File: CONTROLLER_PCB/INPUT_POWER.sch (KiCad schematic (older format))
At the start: 14 parts

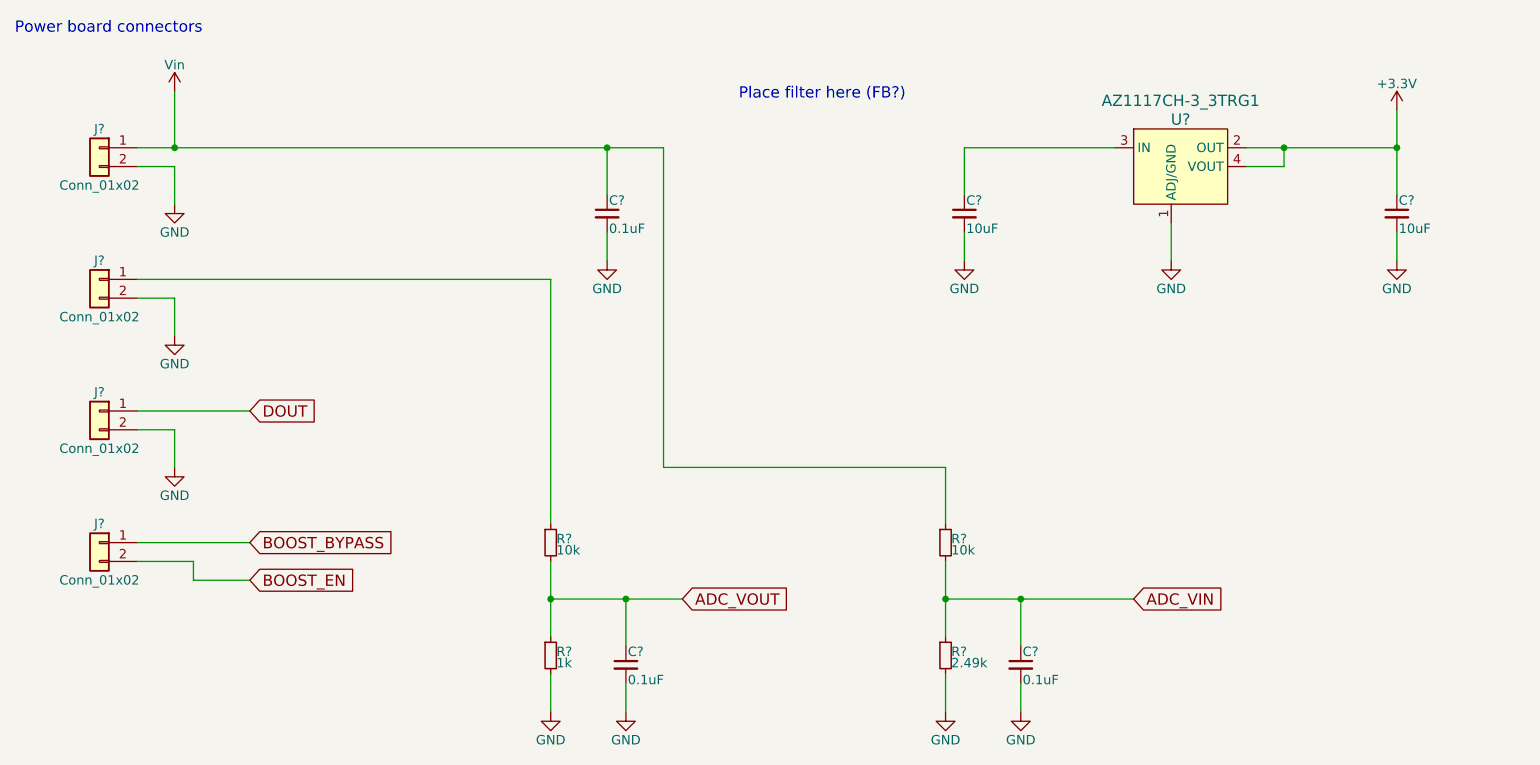
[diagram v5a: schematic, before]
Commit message: Updated POWER_PCB & CONTROLLER_PCB sch's and layouts
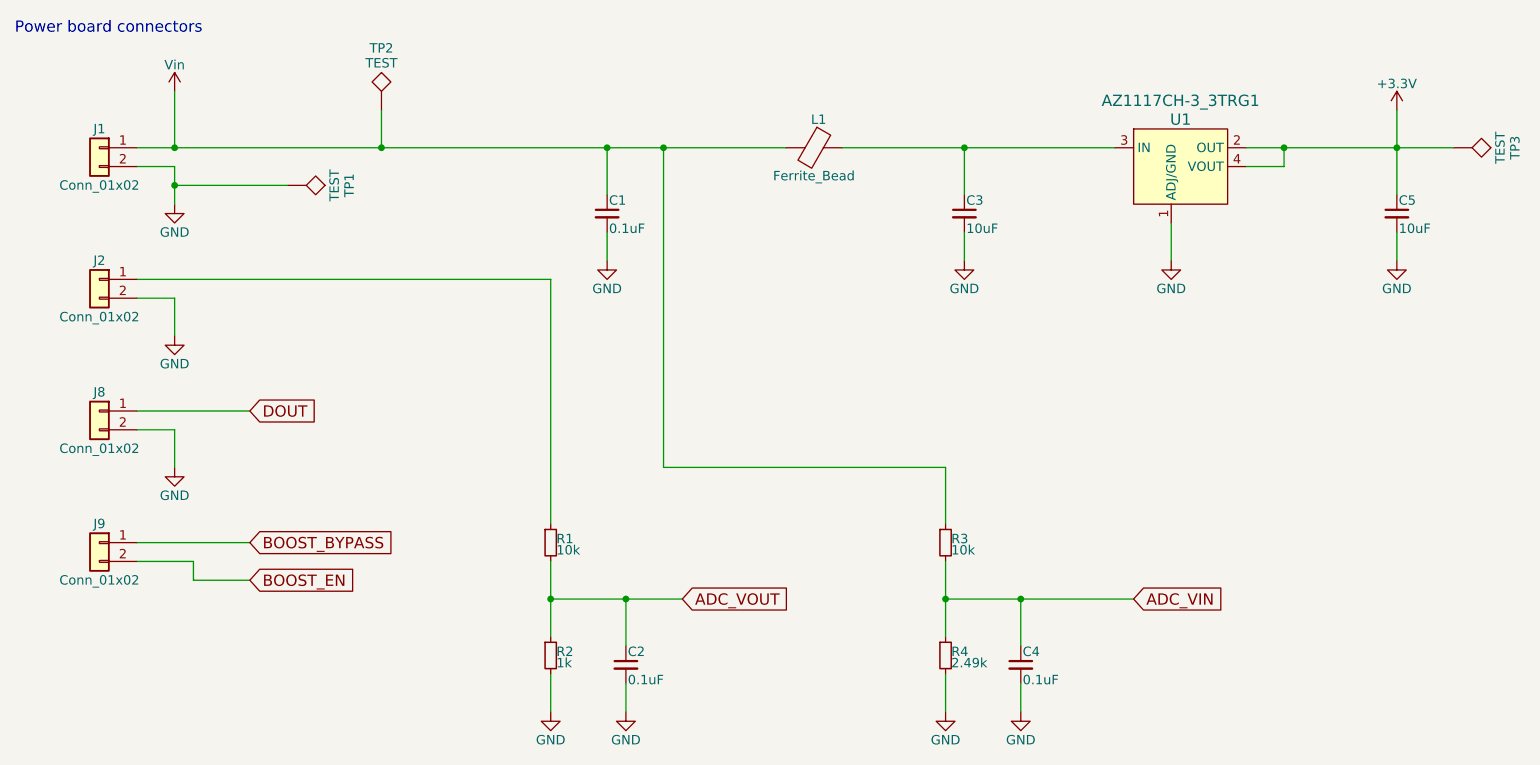
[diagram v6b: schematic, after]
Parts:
- added L1: Ferrite_Bead, Capacitors_SMD:C_0805_HandSoldering, symbol Ferrite_Bead
- added TP1, TP2, TP3: TEST, Measurement_Points:Measurement_Point_Round-SMD-Pad_Small, symbol TEST
- J1, J2, J8, J9: renamed from J?; footprint (none) -> Pin_Headers:Pin_Header_Straight_1x02_Pitch2.54mm
- gave numbers to parts that had none: 10
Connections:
- net +3V3: now also TP3.1
- net GND: now also TP1.1
- net Vin: now also L1.2, TP2.1
- net at C3.1, U1.3 (IN): now also L1.1
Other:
- note removed: "Place filter here (FB?)"
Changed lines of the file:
@@
 $EndDescr
 $Comp
-L Conn_01x02 J?
+L Conn_01x02 J1
 U 1 1 5C71F1FE
 P 2300 1600
-F 0 "J?" H 2300 1700 50  0000 C CNN
+F 0 "J1" H 2300 1700 50  0000 C CNN
 F 1 "Conn_01x02" H 2300 1400 50  0000 C CNN
-F 2 "" H 2300 1600 50  0001 C CNN
+F 2 "Pin_Headers:Pin_Header_Straight_1x02_Pitch2.54mm" H 2300 1600 50  0001 C CNN
 F 3 "" H 2300 1600 50  0001 C CNN
 	1    2300 1600
@@
 $EndComp
 $Comp
-L Conn_01x02 J?
+L Conn_01x02 J2
 U 1 1 5C71F1FF
 P 2300 2300
-F 0 "J?" H 2300 2400 50  0000 C CNN
+F 0 "J2" H 2300 2400 50  0000 C CNN
 F 1 "Conn_01x02" H 2300 2100 50  0000 C CNN
-F 2 "" H 2300 2300 50  0001 C CNN
+F 2 "Pin_Headers:Pin_Header_Straight_1x02_Pitch2.54mm" H 2300 2300 50  0001 C CNN
 F 3 "" H 2300 2300 50  0001 C CNN
 	1    2300 2300
@@
 $EndComp
 $Comp
-L Conn_01x02 J?
+L Conn_01x02 J8
 U 1 1 5C71F200
 P 2300 3000
-F 0 "J?" H 2300 3100 50  0000 C CNN
+F 0 "J8" H 2300 3100 50  0000 C CNN
 F 1 "Conn_01x02" H 2300 2800 50  0000 C CNN
-F 2 "" H 2300 3000 50  0001 C CNN
+F 2 "Pin_Headers:Pin_Header_Straight_1x02_Pitch2.54mm" H 2300 3000 50  0001 C CNN
 F 3 "" H 2300 3000 50  0001 C CNN
 	1    2300 3000
@@
 $EndComp
 $Comp
-L GND #PWR?
+L GND #PWR01
 U 1 1 5C71F201
 P 2700 1900
-F 0 "#PWR?" H 2700 1650 50  0001 C CNN
+F 0 "#PWR01" H 2700 1650 50  0001 C CNN
 F 1 "GND" H 2700 1750 50  0000 C CNN
 F 2 "" H 2700 1900 50  0001 C CNN
@@
 	2700 1700 2700 1900
 $Comp
-L Vin #PWR?
+L Vin #PWR02
 U 1 1 5C71F202
 P 2700 1300
-F 0 "#PWR?" H 2700 1150 50  0001 C CNN
+F 0 "#PWR02" H 2700 1150 50  0001 C CNN
 F 1 "Vin" H 2700 1440 50  0000 C CNN
 F 2 "" H 2700 1300 50  0001 C CNN
@@
 	2700 1300 2700 1600
 $Comp
-L Conn_01x02 J?
+L Conn_01x02 J9
 U 1 1 5C71F203
 P 2300 3700
-F 0 "J?" H 2300 3800 50  0000 C CNN
+F 0 "J9" H 2300 3800 50  0000 C CNN
 F 1 "Conn_01x02" H 2300 3500 50  0000 C CNN
-F 2 "" H 2300 3700 50  0001 C CNN
+F 2 "Pin_Headers:Pin_Header_Straight_1x02_Pitch2.54mm" H 2300 3700 50  0001 C CNN
 F 3 "" H 2300 3700 50  0001 C CNN
 	1    2300 3700
@@
 $EndComp
 $Comp
-L GND #PWR?
+L GND #PWR03
 U 1 1 5C71F204
 P 2700 2600
-F 0 "#PWR?" H 2700 2350 50  0001 C CNN
+F 0 "#PWR03" H 2700 2350 50  0001 C CNN
 F 1 "GND" H 2700 2450 50  0000 C CNN
 F 2 "" H 2700 2600 50  0001 C CNN
@@
 	2700 1700 2500 1700
 Wire Wire Line
-	2500 1600 5300 1600
-$Comp
-L GND #PWR?
+	2500 1600 5950 1600
+$Comp
+L GND #PWR04
 U 1 1 5C71F205
 P 2700 3300
-F 0 "#PWR?" H 2700 3050 50  0001 C CNN
+F 0 "#PWR04" H 2700 3050 50  0001 C CNN
 F 1 "GND" H 2700 3150 50  0000 C CNN
 F 2 "" H 2700 3300 50  0001 C CNN
@@
 Power board connectors
 $Comp
-L AZ1117CH-3_3TRG1 U?
+L AZ1117CH-3_3TRG1 U1
 U 1 1 5C71F57F
 P 8000 1600
-F 0 "U?" H 8050 1750 60  0000 C CNN
+F 0 "U1" H 8050 1750 60  0000 C CNN
 F 1 "AZ1117CH-3_3TRG1" H 8050 1850 60  0000 C CNN
 F 2 "digikey-footprints:SOT-223" H 8200 1800 60  0001 L CNN
@@
 $EndComp
 $Comp
-L C_Small C?
+L C_Small C3
 U 1 1 5C71F6FE
 P 6900 1950
-F 0 "C?" H 6910 2020 50  0000 L CNN
+F 0 "C3" H 6910 2020 50  0000 L CNN
 F 1 "10uF" H 6910 1870 50  0000 L CNN
 F 2 "Capacitors_SMD:C_0805_HandSoldering" H 6900 1950 50  0001 C CNN
@@
 $EndComp
 $Comp
-L GND #PWR?
+L GND #PWR05
 U 1 1 5C71F705
 P 6900 2200
-F 0 "#PWR?" H 6900 1950 50  0001 C CNN
+F 0 "#PWR05" H 6900 1950 50  0001 C CNN
 F 1 "GND" H 6900 2050 50  0000 C CNN
 F 2 "" H 6900 2200 50  0001 C CNN
@@
 $EndComp
 $Comp
-L +3.3V #PWR?
+L +3.3V #PWR06
 U 1 1 5C71F70B
 P 9200 1400
-F 0 "#PWR?" H 9200 1250 50  0001 C CNN
+F 0 "#PWR06" H 9200 1250 50  0001 C CNN
 F 1 "+3.3V" H 9200 1540 50  0000 C CNN
 F 2 "" H 9200 1400 50  0001 C CNN
@@
 	6900 2050 6900 2200
 $Comp
-L C_Small C?
+L C_Small C5
 U 1 1 5C71F7B4
 P 9200 1950
-F 0 "C?" H 9210 2020 50  0000 L CNN
+F 0 "C5" H 9210 2020 50  0000 L CNN
 F 1 "10uF" H 9210 1870 50  0000 L CNN
 F 2 "Capacitors_SMD:C_0805_HandSoldering" H 9200 1950 50  0001 C CNN
@@
 $EndComp
 $Comp
-L GND #PWR?
+L GND #PWR07
 U 1 1 5C71F7BA
 P 9200 2200
-F 0 "#PWR?" H 9200 1950 50  0001 C CNN
+F 0 "#PWR07" H 9200 1950 50  0001 C CNN
 F 1 "GND" H 9200 2050 50  0000 C CNN
 F 2 "" H 9200 2200 50  0001 C CNN
@@
 	9200 2050 9200 2200
 $Comp
-L GND #PWR?
+L GND #PWR08
 U 1 1 5C71F7DD
 P 8000 2200
-F 0 "#PWR?" H 8000 1950 50  0001 C CNN
+F 0 "#PWR08" H 8000 1950 50  0001 C CNN
 F 1 "GND" H 8000 2050 50  0000 C CNN
 F 2 "" H 8000 2200 50  0001 C CNN
@@
 	8000 2000 8000 2200
 Wire Wire Line
-	8400 1600 9200 1600
+	8400 1600 9500 1600
 Connection ~ 9200 1600
 Wire Wire Line
@@
 Connection ~ 8600 1600
 Wire Wire Line
-	7700 1600 6900 1600
-$Comp
-L R_Small R?
+	6250 1600 7700 1600
+$Comp
+L R_Small R1
 U 1 1 5C71FC58
 P 4700 3700
-F 0 "R?" H 4730 3720 50  0000 L CNN
+F 0 "R1" H 4730 3720 50  0000 L CNN
 F 1 "10k" H 4730 3660 50  0000 L CNN
 F 2 "Resistors_SMD:R_0603_HandSoldering" H 4700 3700 50  0001 C CNN
@@
 $EndComp
 $Comp
-L R_Small R?
+L R_Small R2
 U 1 1 5C71FC9D
 P 4700 4300
-F 0 "R?" H 4730 4320 50  0000 L CNN
+F 0 "R2" H 4730 4320 50  0000 L CNN
 F 1 "1k" H 4730 4260 50  0000 L CNN
 F 2 "Resistors_SMD:R_0603_HandSoldering" H 4700 4300 50  0001 C CNN
@@
 $EndComp
 $Comp
-L C_Small C?
+L C_Small C2
 U 1 1 5C71FF06
 P 5100 4350
-F 0 "C?" H 5110 4420 50  0000 L CNN
+F 0 "C2" H 5110 4420 50  0000 L CNN
 F 1 "0.1uF" H 5110 4270 50  0000 L CNN
 F 2 "Capacitors_SMD:C_0603_HandSoldering" H 5100 4350 50  0001 C CNN
@@
 $EndComp
 $Comp
-L GND #PWR?
+L GND #PWR09
 U 1 1 5C71FF0D
 P 5100 4600
-F 0 "#PWR?" H 5100 4350 50  0001 C CNN
+F 0 "#PWR09" H 5100 4350 50  0001 C CNN
 F 1 "GND" H 5100 4450 50  0000 C CNN
 F 2 "" H 5100 4600 50  0001 C CNN
@@
 	5100 4450 5100 4600
 $Comp
-L R_Small R?
+L R_Small R3
 U 1 1 5C72000B
 P 6800 3700
-F 0 "R?" H 6830 3720 50  0000 L CNN
+F 0 "R3" H 6830 3720 50  0000 L CNN
 F 1 "10k" H 6830 3660 50  0000 L CNN
 F 2 "Resistors_SMD:R_0603_HandSoldering" H 6800 3700 50  0001 C CNN
@@
 $EndComp
 $Comp
-L R_Small R?
+L R_Small R4
 U 1 1 5C720011
 P 6800 4300
-F 0 "R?" H 6830 4320 50  0000 L CNN
+F 0 "R4" H 6830 4320 50  0000 L CNN
 F 1 "2.49k" H 6830 4260 50  0000 L CNN
 F 2 "Resistors_SMD:R_0603_HandSoldering" H 6800 4300 50  0001 C CNN
@@
 $EndComp
 $Comp
-L C_Small C?
+L C_Small C4
 U 1 1 5C720017
 P 7200 4350
-F 0 "C?" H 7210 4420 50  0000 L CNN
+F 0 "C4" H 7210 4420 50  0000 L CNN
 F 1 "0.1uF" H 7210 4270 50  0000 L CNN
 F 2 "Capacitors_SMD:C_0603_HandSoldering" H 7200 4350 50  0001 C CNN
@@
 $EndComp
 $Comp
-L GND #PWR?
+L GND #PWR010
 U 1 1 5C72001D
 P 7200 4600
-F 0 "#PWR?" H 7200 4350 50  0001 C CNN
+F 0 "#PWR010" H 7200 4350 50  0001 C CNN
 F 1 "GND" H 7200 4450 50  0000 C CNN
 F 2 "" H 7200 4600 50  0001 C CNN
@@
 	4700 2300 4700 3600
 $Comp
-L GND #PWR?
+L GND #PWR011
 U 1 1 5C720067
 P 4700 4600
-F 0 "#PWR?" H 4700 4350 50  0001 C CNN
+F 0 "#PWR011" H 4700 4350 50  0001 C CNN
 F 1 "GND" H 4700 4450 50  0000 C CNN
 F 2 "" H 4700 4600 50  0001 C CNN
@@
 	4700 4400 4700 4600
 $Comp
-L GND #PWR?
+L GND #PWR012
 U 1 1 5C7200E7
 P 6800 4600
-F 0 "#PWR?" H 6800 4350 50  0001 C CNN
+F 0 "#PWR012" H 6800 4350 50  0001 C CNN
 F 1 "GND" H 6800 4450 50  0000 C CNN
 F 2 "" H 6800 4600 50  0001 C CNN
@@
 Connection ~ 2700 1600
 $Comp
-L C_Small C?
+L C_Small C1
 U 1 1 5C7202FB
 P 5000 1950
-F 0 "C?" H 5010 2020 50  0000 L CNN
+F 0 "C1" H 5010 2020 50  0000 L CNN
 F 1 "0.1uF" H 5010 1870 50  0000 L CNN
 F 2 "Capacitors_SMD:C_0603_HandSoldering" H 5000 1950 50  0001 C CNN
@@
 $EndComp
 $Comp
-L GND #PWR?
+L GND #PWR013
 U 1 1 5C720302
 P 5000 2200
-F 0 "#PWR?" H 5000 1950 50  0001 C CNN
+F 0 "#PWR013" H 5000 1950 50  0001 C CNN
 F 1 "GND" H 5000 2050 50  0000 C CNN
 F 2 "" H 5000 2200 50  0001 C CNN
@@
 ADC_VIN
 Connection ~ 7200 4000
-Text Notes 5700 1350 0    60   ~ 0
-Place filter here (FB?)
+$Comp
+L Ferrite_Bead L1
+U 1 1 5C720EF4
+P 6100 1600
+F 0 "L1" V 5950 1625 50  0000 C CNN
+F 1 "Ferrite_Bead" V 6250 1600 50  0000 C CNN
+F 2 "Capacitors_SMD:C_0805_HandSoldering" V 6030 1600 50  0001 C CNN
+F 3 "" H 6100 1600 50  0001 C CNN
+	1    6100 1600
+	0    1    1    0
+$EndComp
+Connection ~ 5300 1600
+Connection ~ 6900 1600
+$Comp
+L TEST TP3
+U 1 1 5C725923
+P 9500 1600
+F 0 "TP3" H 9500 1900 50  0000 C BNN
+F 1 "TEST" H 9500 1850 50  0000 C CNN
+F 2 "Measurement_Points:Measurement_Point_Round-SMD-Pad_Small" H 9500 1600 50  0001 C CNN
+F 3 "" H 9500 1600 50  0001 C CNN
+	1    9500 1600
+	0    1    1    0
+$EndComp
+$Comp
+L TEST TP2
+U 1 1 5C7259B0
+P 3800 1400
+F 0 "TP2" H 3800 1700 50  0000 C BNN
+F 1 "TEST" H 3800 1650 50  0000 C CNN
+F 2 "Measurement_Points:Measurement_Point_Round-SMD-Pad_Small" H 3800 1400 50  0001 C CNN
+F 3 "" H 3800 1400 50  0001 C CNN
+	1    3800 1400
+	1    0    0    -1
+$EndComp
+$Comp
+L TEST TP1
+U 1 1 5C725B03
+P 3300 1800
+F 0 "TP1" H 3300 2100 50  0000 C BNN
+F 1 "TEST" H 3300 2050 50  0000 C CNN
+F 2 "Measurement_Points:Measurement_Point_Round-SMD-Pad_Small" H 3300 1800 50  0001 C CNN
+F 3 "" H 3300 1800 50  0001 C CNN
+	1    3300 1800
+	0    1    1    0
+$EndComp
+Wire Wire Line
+	3300 1800 2700 1800
+Connection ~ 2700 1800
+Wire Wire Line
+	3800 1400 3800 1600
+Connection ~ 3800 1600
 $EndSCHEMATC
